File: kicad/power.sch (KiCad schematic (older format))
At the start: 16 parts

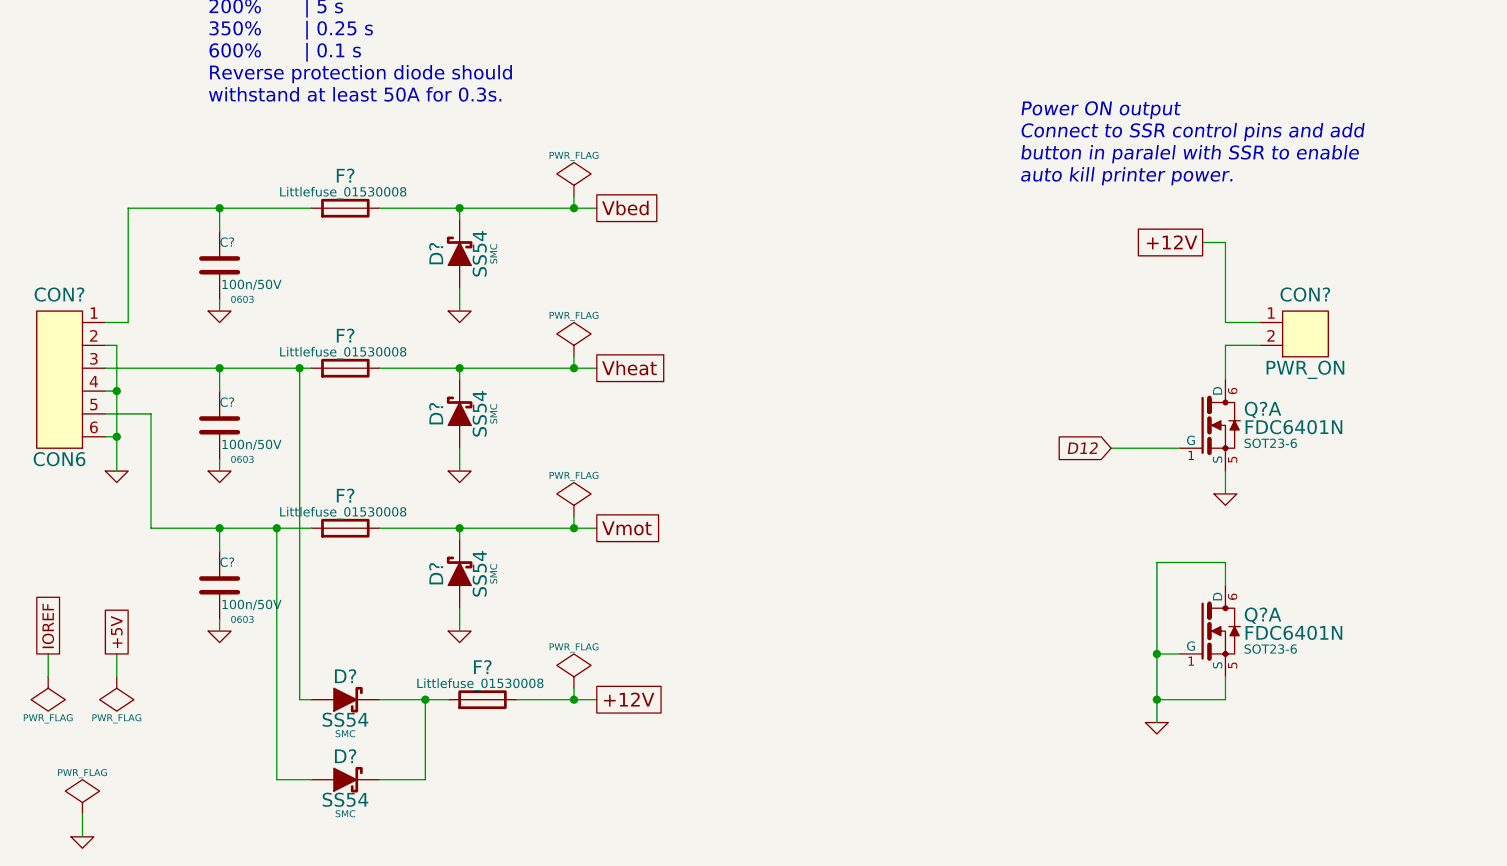
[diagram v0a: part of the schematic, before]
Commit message: Add AUX connectro for a few buttons or so
close #14
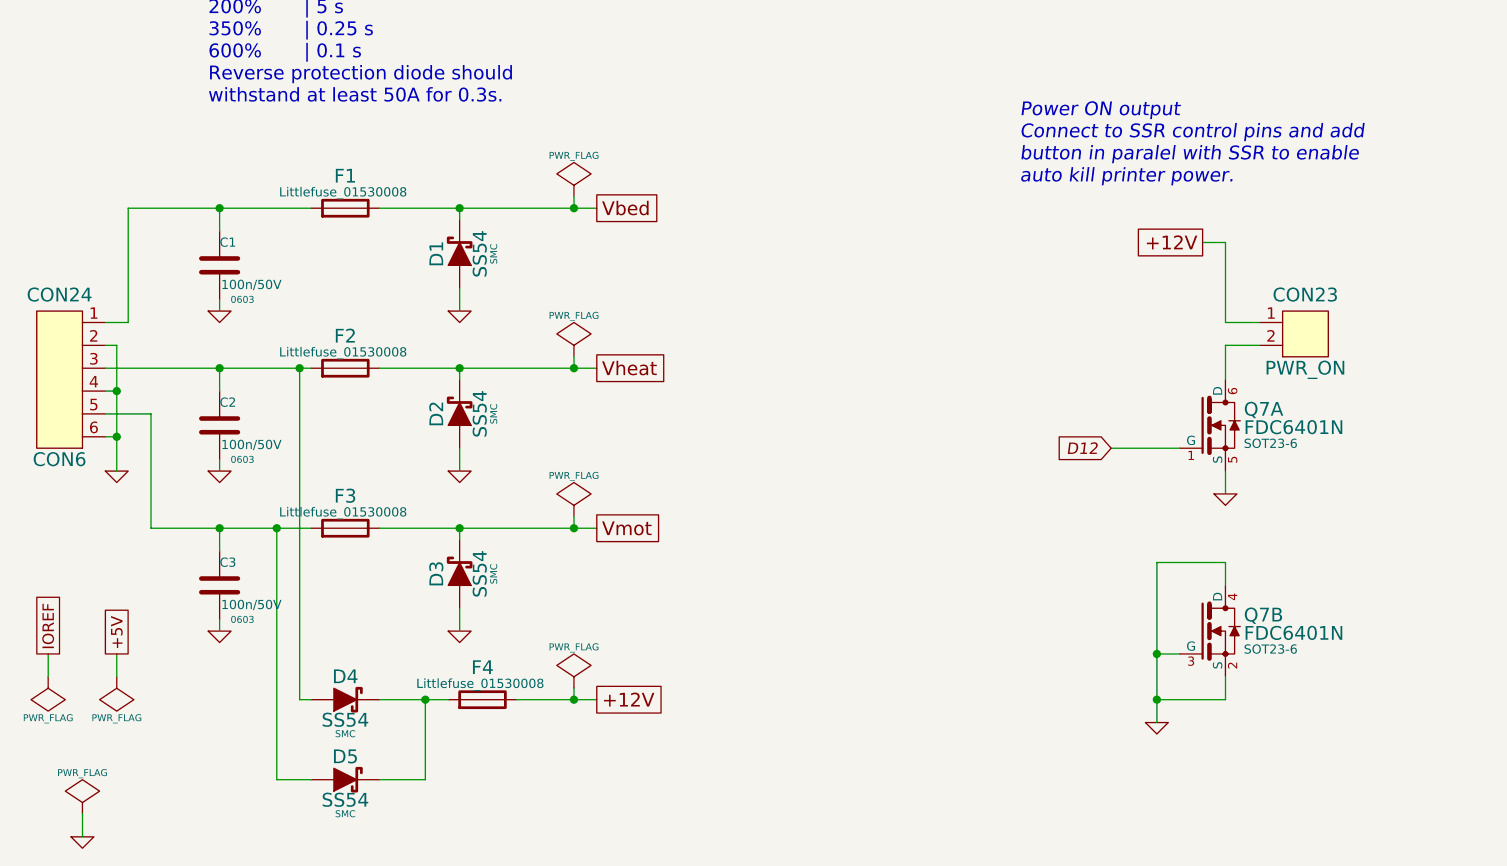
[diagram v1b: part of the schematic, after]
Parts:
- gave numbers to parts that had none: 15
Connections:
- net GND: now also Q7.2 (S), Q7.3 (G), Q7.4 (D); no longer Q7.1 (G), Q7.5 (S), Q7.6 (D)
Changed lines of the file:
@@
 $EndDescr
 $Comp
-L GND #PWR?
+L GND #PWR58
 U 1 1 53943822
 P 1400 3250
-F 0 "#PWR?" H 1400 3250 30  0001 C CNN
+F 0 "#PWR58" H 1400 3250 30  0001 C CNN
 F 1 "GND" H 1400 3180 30  0001 C CNN
 F 2 "" H 1400 3250 60  0000 C CNN
@@
 Littelfuse MINI Blade Fuse\nmodel 0297015 (15A)\n% of rating | opening time max\n135%       | 600s\n200%       | 5 s \n350%       | 0.25 s \n600%       | 0.1 s\nReverse protection diode should \nwithstand at least 50A for 0.3s.
 $Comp
-L GND #PWR?
+L GND #PWR60
 U 1 1 53943829
 P 2900 3250
-F 0 "#PWR?" H 2900 3250 30  0001 C CNN
+F 0 "#PWR60" H 2900 3250 30  0001 C CNN
 F 1 "GND" H 2900 3180 30  0001 C CNN
 F 2 "" H 2900 3250 60  0000 C CNN
@@
 $EndComp
 $Comp
-L GND #PWR?
+L GND #PWR57
 U 1 1 5394382F
 P 2900 2550
-F 0 "#PWR?" H 2900 2550 30  0001 C CNN
+F 0 "#PWR57" H 2900 2550 30  0001 C CNN
 F 1 "GND" H 2900 2480 30  0001 C CNN
 F 2 "" H 2900 2550 60  0000 C CNN
@@
 $EndComp
 $Comp
-L GND #PWR?
+L GND #PWR63
 U 1 1 53943835
 P 2900 3950
-F 0 "#PWR?" H 2900 3950 30  0001 C CNN
+F 0 "#PWR63" H 2900 3950 30  0001 C CNN
 F 1 "GND" H 2900 3880 30  0001 C CNN
 F 2 "" H 2900 3950 60  0000 C CNN
@@
 $EndComp
 $Comp
-L C C?
+L C C1
 U 1 1 5394383B
 P 1850 2350
-F 0 "C?" H 1850 2450 40  0000 L CNN
+F 0 "C1" H 1850 2450 40  0000 L CNN
 F 1 "100n/50V" H 1856 2265 40  0000 L CNN
 F 2 "0603" H 1950 2200 30  0000 C CNN
@@
 $EndComp
 $Comp
-L GND #PWR?
+L GND #PWR56
 U 1 1 53943842
 P 1850 2550
-F 0 "#PWR?" H 1850 2550 30  0001 C CNN
+F 0 "#PWR56" H 1850 2550 30  0001 C CNN
 F 1 "GND" H 1850 2480 30  0001 C CNN
 F 2 "" H 1850 2550 60  0000 C CNN
@@
 $EndComp
 $Comp
-L GND #PWR?
+L GND #PWR59
 U 1 1 53943848
 P 1850 3250
-F 0 "#PWR?" H 1850 3250 30  0001 C CNN
+F 0 "#PWR59" H 1850 3250 30  0001 C CNN
 F 1 "GND" H 1850 3180 30  0001 C CNN
 F 2 "" H 1850 3250 60  0000 C CNN
@@
 $EndComp
 $Comp
-L GND #PWR?
+L GND #PWR62
 U 1 1 5394384E
 P 1850 3950
-F 0 "#PWR?" H 1850 3950 30  0001 C CNN
+F 0 "#PWR62" H 1850 3950 30  0001 C CNN
 F 1 "GND" H 1850 3880 30  0001 C CNN
 F 2 "" H 1850 3950 60  0000 C CNN
@@
 $EndComp
 $Comp
-L C C?
+L C C2
 U 1 1 53943854
 P 1850 3050
-F 0 "C?" H 1850 3150 40  0000 L CNN
+F 0 "C2" H 1850 3150 40  0000 L CNN
 F 1 "100n/50V" H 1856 2965 40  0000 L CNN
 F 2 "0603" H 1950 2900 30  0000 C CNN
@@
 $EndComp
 $Comp
-L C C?
+L C C3
 U 1 1 5394385B
 P 1850 3750
-F 0 "C?" H 1850 3850 40  0000 L CNN
+F 0 "C3" H 1850 3850 40  0000 L CNN
 F 1 "100n/50V" H 1856 3665 40  0000 L CNN
 F 2 "0603" H 1950 3600 30  0000 C CNN
@@
 Vmot
 $Comp
-L SS54 D?
+L SS54 D1
 U 1 1 53943865
 P 2900 2300
-F 0 "D?" H 2900 2200 60  0000 C CNN
+F 0 "D1" H 2900 2200 60  0000 C CNN
 F 1 "SS54" H 2900 2390 60  0000 C CNN
 F 2 "SMC" H 2900 2450 30  0000 C CNN
@@
 $EndComp
 $Comp
-L SS54 D?
+L SS54 D2
 U 1 1 5394386C
 P 2900 3000
-F 0 "D?" H 2900 2900 60  0000 C CNN
+F 0 "D2" H 2900 2900 60  0000 C CNN
 F 1 "SS54" H 2900 3090 60  0000 C CNN
 F 2 "SMC" H 2900 3150 30  0000 C CNN
@@
 $EndComp
 $Comp
-L SS54 D?
+L SS54 D3
 U 1 1 53943873
 P 2900 3700
-F 0 "D?" H 2900 3600 60  0000 C CNN
+F 0 "D3" H 2900 3600 60  0000 C CNN
 F 1 "SS54" H 2900 3790 60  0000 C CNN
 F 2 "SMC" H 2900 3850 30  0000 C CNN
@@
 $EndComp
 $Comp
-L SS54 D?
+L SS54 D4
 U 1 1 5394387A
 P 2400 4250
-F 0 "D?" H 2400 4150 60  0000 C CNN
+F 0 "D4" H 2400 4150 60  0000 C CNN
 F 1 "SS54" H 2400 4340 60  0000 C CNN
 F 2 "SMC" H 2400 4400 30  0000 C CNN
@@
 $EndComp
 $Comp
-L SS54 D?
+L SS54 D5
 U 1 1 53943881
 P 2400 4600
-F 0 "D?" H 2400 4500 60  0000 C CNN
+F 0 "D5" H 2400 4500 60  0000 C CNN
 F 1 "SS54" H 2400 4690 60  0000 C CNN
 F 2 "SMC" H 2400 4750 30  0000 C CNN
@@
 $EndComp
 $Comp
-L MINI_Blade_Fuse_Holder F?
+L MINI_Blade_Fuse_Holder F1
 U 1 1 53943888
 P 2400 2100
-F 0 "F?" H 2400 2240 60  0000 C CNN
+F 0 "F1" H 2400 2240 60  0000 C CNN
 F 1 "MINI_Blade_Fuse_Holder" H 2400 2015 60  0001 C CNN
 F 2 "Littlefuse_01530008" H 2390 2170 40  0000 C CNN
@@
 $EndComp
 $Comp
-L MINI_Blade_Fuse_Holder F?
+L MINI_Blade_Fuse_Holder F2
 U 1 1 5394388F
 P 2400 2800
-F 0 "F?" H 2400 2940 60  0000 C CNN
+F 0 "F2" H 2400 2940 60  0000 C CNN
 F 1 "MINI_Blade_Fuse_Holder" H 2400 2715 60  0001 C CNN
 F 2 "Littlefuse_01530008" H 2390 2870 40  0000 C CNN
@@
 $EndComp
 $Comp
-L MINI_Blade_Fuse_Holder F?
+L MINI_Blade_Fuse_Holder F3
 U 1 1 53943896
 P 2400 3500
-F 0 "F?" H 2400 3640 60  0000 C CNN
+F 0 "F3" H 2400 3640 60  0000 C CNN
 F 1 "MINI_Blade_Fuse_Holder" H 2400 3415 60  0001 C CNN
 F 2 "Littlefuse_01530008" H 2390 3570 40  0000 C CNN
@@
 $EndComp
 $Comp
-L MINI_Blade_Fuse_Holder F?
+L MINI_Blade_Fuse_Holder F4
 U 1 1 5394389D
 P 3000 4250
-F 0 "F?" H 3000 4390 60  0000 C CNN
+F 0 "F4" H 3000 4390 60  0000 C CNN
 F 1 "MINI_Blade_Fuse_Holder" H 3000 4165 60  0001 C CNN
 F 2 "Littlefuse_01530008" H 2990 4320 40  0000 C CNN
@@
 +12V
 $Comp
-L CON6 CON?
+L CON6 CON24
 U 1 1 539438A5
 P 1150 2850
-F 0 "CON?" H 1150 3220 60  0000 C CNN
+F 0 "CON24" H 1150 3220 60  0000 C CNN
 F 1 "CON6" H 1150 2500 60  0000 C CNN
 F 2 "" H 1150 2850 40  0000 C CNN
@@
 $EndComp
 $Comp
-L PWR_FLAG #FLG?
+L PWR_FLAG #FLG1
 U 1 1 539438AC
 P 3400 2050
-F 0 "#FLG?" H 3400 2145 30  0001 C CNN
+F 0 "#FLG1" H 3400 2145 30  0001 C CNN
 F 1 "PWR_FLAG" H 3400 2230 30  0000 C CNN
 F 2 "" H 3400 2050 60  0000 C CNN
@@
 $EndComp
 $Comp
-L PWR_FLAG #FLG?
+L PWR_FLAG #FLG2
 U 1 1 539438B2
 P 3400 2750
-F 0 "#FLG?" H 3400 2845 30  0001 C CNN
+F 0 "#FLG2" H 3400 2845 30  0001 C CNN
 F 1 "PWR_FLAG" H 3400 2930 30  0000 C CNN
 F 2 "" H 3400 2750 60  0000 C CNN
@@
 $EndComp
 $Comp
-L PWR_FLAG #FLG?
+L PWR_FLAG #FLG3
 U 1 1 539438B8
 P 3400 3450
-F 0 "#FLG?" H 3400 3545 30  0001 C CNN
+F 0 "#FLG3" H 3400 3545 30  0001 C CNN
 F 1 "PWR_FLAG" H 3400 3630 30  0000 C CNN
 F 2 "" H 3400 3450 60  0000 C CNN
@@
 $EndComp
 $Comp
-L PWR_FLAG #FLG?
+L PWR_FLAG #FLG6
 U 1 1 539438BE
 P 3400 4200
-F 0 "#FLG?" H 3400 4295 30  0001 C CNN
+F 0 "#FLG6" H 3400 4295 30  0001 C CNN
 F 1 "PWR_FLAG" H 3400 4380 30  0000 C CNN
 F 2 "" H 3400 4200 60  0000 C CNN
@@
 $EndComp
 $Comp
-L PWR_FLAG #FLG?
+L PWR_FLAG #FLG7
 U 1 1 539438C4
 P 1250 4750
-F 0 "#FLG?" H 1250 4845 30  0001 C CNN
+F 0 "#FLG7" H 1250 4845 30  0001 C CNN
 F 1 "PWR_FLAG" H 1250 4930 30  0000 C CNN
 F 2 "" H 1250 4750 60  0000 C CNN
@@
 $EndComp
 $Comp
-L GND #PWR?
+L GND #PWR65
 U 1 1 539438CA
 P 1250 4850
-F 0 "#PWR?" H 1250 4850 30  0001 C CNN
+F 0 "#PWR65" H 1250 4850 30  0001 C CNN
 F 1 "GND" H 1250 4780 30  0001 C CNN
 F 2 "" H 1250 4850 60  0000 C CNN
@@
 IOREF
 $Comp
-L PWR_FLAG #FLG?
+L PWR_FLAG #FLG5
 U 1 1 53943908
 P 1400 4150
-F 0 "#FLG?" H 1400 4245 30  0001 C CNN
+F 0 "#FLG5" H 1400 4245 30  0001 C CNN
 F 1 "PWR_FLAG" H 1400 4330 30  0000 C CNN
 F 2 "" H 1400 4150 60  0000 C CNN
@@
 $EndComp
 $Comp
-L PWR_FLAG #FLG?
+L PWR_FLAG #FLG4
 U 1 1 5394390F
 P 1100 4150
-F 0 "#FLG?" H 1100 4245 30  0001 C CNN
+F 0 "#FLG4" H 1100 4245 30  0001 C CNN
 F 1 "PWR_FLAG" H 1100 4330 30  0000 C CNN
 F 2 "" H 1100 4150 60  0000 C CNN
@@
 $EndComp
 $Comp
-L CON2 CON?
+L CON2 CON23
 U 1 1 53943916
 P 6600 2650
-F 0 "CON?" H 6600 2820 60  0000 C CNN
+F 0 "CON23" H 6600 2820 60  0000 C CNN
 F 1 "PWR_ON" H 6600 2500 60  0000 C CNN
 F 2 "" H 6600 2650 40  0000 C CNN
@@
 $EndComp
 $Comp
-L FDC6401N Q?
+L FDC6401N Q7
 U 1 1 5394391D
 P 6150 3050
-F 0 "Q?" H 6330 3120 60  0000 L CNN
+F 0 "Q7" H 6330 3120 60  0000 L CNN
 F 1 "FDC6401N" H 6330 3040 60  0000 L CNN
 F 2 "SOT23-6" H 6330 2970 40  0000 L CNN
@@
 $EndComp
 $Comp
-L FDC6401N Q?
-U 1 1 53943924
+L FDC6401N Q7
+U 2 1 53943924
 P 6150 3950
-F 0 "Q?" H 6330 4020 60  0000 L CNN
+F 0 "Q7" H 6330 4020 60  0000 L CNN
 F 1 "FDC6401N" H 6330 3940 60  0000 L CNN
 F 2 "SOT23-6" H 6330 3870 40  0000 L CNN
 F 3 "" H 6150 3900 60  0000 C CNN
-	1    6150 3950
-	1    0    0    -1
-$EndComp
-$Comp
-L GND #PWR?
+	2    6150 3950
+	1    0    0    -1
+$EndComp
+$Comp
+L GND #PWR64
 U 1 1 53943ED6
 P 5950 4350
-F 0 "#PWR?" H 5950 4350 30  0001 C CNN
+F 0 "#PWR64" H 5950 4350 30  0001 C CNN
 F 1 "GND" H 5950 4280 30  0001 C CNN
 F 2 "" H 5950 4350 60  0000 C CNN
@@
 $EndComp
 $Comp
-L GND #PWR?
+L GND #PWR61
 U 1 1 53943F43
 P 6250 3350
-F 0 "#PWR?" H 6250 3350 30  0001 C CNN
+F 0 "#PWR61" H 6250 3350 30  0001 C CNN
 F 1 "GND" H 6250 3280 30  0001 C CNN
 F 2 "" H 6250 3350 60  0000 C CNN
